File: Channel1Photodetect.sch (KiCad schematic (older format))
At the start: 9 parts, among them U201 MCP6404, U202 LM339

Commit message: revised feedback resistor and updated reference voltage divider
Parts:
- removed R202: 22M, Resistors_SMD:R_0805_HandSoldering, symbol R_Small
- C202: value 2.2p -> 50p; Fieldname (none) -> Value
- R201: value 22M -> 2M; Fieldname (none) -> Value; MPN RMCF0805FT22M0 -> (none)
- renumbered R203 to R202
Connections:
- net at R201.1: now also C202.1, R202.2, U201.1, U202.5 (+)
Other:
- moved on the sheet: R201
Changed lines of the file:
@@
 L R_Small R201
 U 1 1 58228B7C
-P 5040 2480
-F 0 "R201" V 5120 2440 50  0000 L CNN
-F 1 "22M" V 4970 2360 50  0000 L CNN
-F 2 "Resistors_SMD:R_0805_HandSoldering" H 5040 2480 50  0001 C CNN
-F 3 "" H 5040 2480 50  0000 C CNN
-F 4 "RMCF0805FT22M0" H 5040 2480 60  0001 C CNN "MPN"
-	1    5040 2480
+P 5280 2480
+F 0 "R201" V 5360 2440 50  0000 L CNN
+F 1 "2M" V 5210 2360 50  0000 L CNN
+F 2 "Resistors_SMD:R_0805_HandSoldering" H 5280 2480 50  0001 C CNN
+F 3 "" H 5280 2480 50  0000 C CNN
+F 4 "Value" H 5280 2480 60  0001 C CNN "Fieldname"
+	1    5280 2480
 	0    1    1    0
 $EndComp
@@
 P 5270 1990
 F 0 "C202" V 5390 1950 50  0000 L CNN
-F 1 "2.2p" V 5160 1860 50  0000 L CNN
+F 1 "50p" V 5160 1860 50  0000 L CNN
 F 2 "Capacitors_SMD:C_0805_HandSoldering" H 5270 1990 50  0001 C CNN
 F 3 "" H 5270 1990 50  0000 C CNN
+F 4 "Value" H 5270 1990 60  0001 C CNN "Fieldname"
 	1    5270 1990
 	0    1    1    0
@@
 	4860 3140 4860 3440
 $Comp
-L R_Small R203
+L R_Small R202
 U 1 1 58228BA3
 P 5670 3440
-F 0 "R203" V 5750 3400 50  0000 L CNN
+F 0 "R202" V 5750 3400 50  0000 L CNN
 F 1 "10K" V 5600 3320 50  0000 L CNN
 F 2 "Resistors_SMD:R_0805_HandSoldering" H 5670 3440 50  0001 C CNN
@@
 Wire Wire Line
 	6820 3140 7070 3140
-$Comp
-L R_Small R202
-U 1 1 5823C31A
-P 5370 2480
-F 0 "R202" V 5450 2440 50  0000 L CNN
-F 1 "22M" V 5300 2360 50  0000 L CNN
-F 2 "Resistors_SMD:R_0805_HandSoldering" H 5370 2480 50  0001 C CNN
-F 3 "" H 5370 2480 50  0000 C CNN
-F 4 "RMCF0805FT22M0" H 5370 2480 60  0001 C CNN "MPN"
-	1    5370 2480
-	0    1    1    0
-$EndComp
-Wire Wire Line
-	5470 2480 5670 2480
 Connection ~ 5670 2480
 Wire Wire Line
-	5270 2480 5140 2480
-Wire Wire Line
-	4940 2480 4860 2480
+	5670 2480 5380 2480
+Wire Wire Line
+	5180 2480 4860 2480
 Connection ~ 4860 2480
 $EndSCHEMATC

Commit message: added pull-up resistors
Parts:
- added R203: 10K, Resistors_SMD:R_0805_HandSoldering, symbol R_Small
- R201: Fieldname Value -> (none); MPN (none) -> RC0805FR-072ML
- U202: Fieldname (none) -> Value; MPN (none) -> LM339DE4
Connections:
- net +3V: now also R203.2
- net PD1: now also R203.1
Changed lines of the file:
@@
 F 2 "Resistors_SMD:R_0805_HandSoldering" H 5280 2480 50  0001 C CNN
 F 3 "" H 5280 2480 50  0000 C CNN
-F 4 "Value" H 5280 2480 60  0001 C CNN "Fieldname"
+F 4 "RC0805FR-072ML" H 5280 2480 60  0001 C CNN "MPN"
 	1    5280 2480
 	0    1    1    0
@@
 F 1 "LM339" H 6620 2940 50  0000 C CNN
 F 2 "Housings_SOIC:SOIC-14_3.9x8.7mm_Pitch1.27mm" H 6470 3240 50  0001 C CNN
-F 3 "" H 6570 3340 50  0000 C CNN
+F 3 "http://www.ti.com/lit/ds/symlink/lm139a.pdf" H 6570 3340 50  0001 C CNN
+F 4 "Value" H 6520 3140 60  0001 C CNN "Fieldname"
+F 5 "LM339DE4" H 6520 3140 60  0001 C CNN "MPN"
 	1    6520 3140
 	1    0    0    -1
@@
 	5180 2480 4860 2480
 Connection ~ 4860 2480
+$Comp
+L R_Small R203
+U 1 1 5824D012
+P 6990 2890
+F 0 "R203" V 7070 2850 50  0000 L CNN
+F 1 "10K" V 6920 2770 50  0000 L CNN
+F 2 "Resistors_SMD:R_0805_HandSoldering" H 6990 2890 50  0001 C CNN
+F 3 "" H 6990 2890 50  0000 C CNN
+F 4 "RC0805FR-072ML" H 6990 2890 60  0001 C CNN "MPN"
+	1    6990 2890
+	-1   0    0    1
+$EndComp
+Text GLabel 6990 2640 1    60   Input ~ 0
++3V
+Wire Wire Line
+	6990 2640 6990 2790
+Wire Wire Line
+	6990 2990 6990 3140
+Connection ~ 6990 3140
 $EndSCHEMATC

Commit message: removed 10K resistors used as load for op amps
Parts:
- removed R202: 10K, Resistors_SMD:R_0805_HandSoldering, symbol R_Small
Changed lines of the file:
@@
 	5170 1990 4860 1990
-Wire Wire Line
-	5670 1990 5670 3340
 Wire Wire Line
 	5460 3040 6220 3040
@@
 	4860 3140 4860 3440
 $Comp
-L R_Small R202
-U 1 1 58228BA3
-P 5670 3440
-F 0 "R202" V 5750 3400 50  0000 L CNN
-F 1 "10K" V 5600 3320 50  0000 L CNN
-F 2 "Resistors_SMD:R_0805_HandSoldering" H 5670 3440 50  0001 C CNN
-F 3 "" H 5670 3440 50  0000 C CNN
-F 4 "Value" H 5670 3440 60  0001 C CNN "Fieldname"
-	1    5670 3440
-	-1   0    0    1
-$EndComp
-Connection ~ 5670 3040
-$Comp
-L GND #PWR06
-U 1 1 58228BAB
-P 5670 3640
-F 0 "#PWR06" H 5670 3390 50  0001 C CNN
-F 1 "GND" H 5670 3490 50  0000 C CNN
-F 2 "" H 5670 3640 50  0000 C CNN
-F 3 "" H 5670 3640 50  0000 C CNN
-	1    5670 3640
-	1    0    0    -1
-$EndComp
-Wire Wire Line
-	5670 3540 5670 3640
-$Comp
 L LM339 U202
 U 1 1 58228BB2
@@
 $EndComp
 $Comp
-L GND #PWR07
+L GND #PWR06
 U 1 1 58228BCA
 P 5060 3450
-F 0 "#PWR07" H 5060 3200 50  0001 C CNN
+F 0 "#PWR06" H 5060 3200 50  0001 C CNN
 F 1 "GND" H 5060 3300 50  0000 C CNN
 F 2 "" H 5060 3450 50  0000 C CNN
@@
 $EndComp
 $Comp
-L GND #PWR08
+L GND #PWR07
 U 1 1 58228BD8
 P 4170 2540
-F 0 "#PWR08" H 4170 2290 50  0001 C CNN
+F 0 "#PWR07" H 4170 2290 50  0001 C CNN
 F 1 "GND" H 4170 2390 50  0000 C CNN
 F 2 "" H 4170 2540 50  0000 C CNN
@@
 	4250 2940 4860 2940
 $Comp
-L GND #PWR09
+L GND #PWR08
 U 1 1 58228BED
 P 4300 3400
-F 0 "#PWR09" H 4300 3150 50  0001 C CNN
+F 0 "#PWR08" H 4300 3150 50  0001 C CNN
 F 1 "GND" H 4300 3250 50  0000 C CNN
 F 2 "" H 4300 3400 50  0000 C CNN
@@
 +3V
 $Comp
-L GND #PWR010
+L GND #PWR09
 U 1 1 58228BF6
 P 6420 3440
-F 0 "#PWR010" H 6420 3190 50  0001 C CNN
+F 0 "#PWR09" H 6420 3190 50  0001 C CNN
 F 1 "GND" H 6420 3290 50  0000 C CNN
 F 2 "" H 6420 3440 50  0000 C CNN
@@
 $EndComp
 $Comp
-L GND #PWR011
+L GND #PWR010
 U 1 1 58228C05
 P 5980 2550
-F 0 "#PWR011" H 5980 2300 50  0001 C CNN
+F 0 "#PWR010" H 5980 2300 50  0001 C CNN
 F 1 "GND" H 5980 2400 50  0000 C CNN
 F 2 "" H 5980 2550 50  0000 C CNN
@@
 Wire Wire Line
 	6820 3140 7070 3140
-Connection ~ 5670 2480
-Wire Wire Line
-	5670 2480 5380 2480
 Wire Wire Line
 	5180 2480 4860 2480
@@
 	6990 2990 6990 3140
 Connection ~ 6990 3140
+Wire Wire Line
+	5380 2480 5680 2480
+Wire Wire Line
+	5680 2480 5680 3040
+Connection ~ 5680 3040
+Wire Wire Line
+	5670 1990 5670 2480
+Connection ~ 5670 2480
 $EndSCHEMATC

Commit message: replaced potentiometer with trimpot
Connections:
- net GND: now also U201.13 (-); no longer U201.2 (-)
- net at C202.1, R201.1, U202.5 (+): now also U201.14; no longer U201.1
- net at C202.2, PD201.1 (K), R201.2: now also U201.12 (+); no longer U201.3 (+)
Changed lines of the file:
@@
 $Comp
 L MCP6404 U201
-U 1 1 58228B8A
+U 4 1 58228B8A
 P 5160 3040
 F 0 "U201" H 5210 3240 50  0000 C CNN
@@
 F 4 "MCP6404-E/SL" H 5160 3040 60  0001 C CNN "MPN"
 F 5 "Value" H 5160 3040 60  0001 C CNN "Fieldname"
-	1    5160 3040
+	4    5160 3040
 	1    0    0    -1
 $EndComp

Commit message: completed pcb basic layout
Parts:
- renumbered R203 to R202
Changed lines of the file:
@@
 	5370 1990 5670 1990
 $Comp
-L GND #PWR05
+L GND #PWR203
 U 1 1 58228B9B
 P 4860 3440
-F 0 "#PWR05" H 4860 3190 50  0001 C CNN
+F 0 "#PWR203" H 4860 3190 50  0001 C CNN
 F 1 "GND" H 4860 3290 50  0000 C CNN
 F 2 "" H 4860 3440 50  0000 C CNN
@@
 $EndComp
 $Comp
-L GND #PWR06
+L GND #PWR204
 U 1 1 58228BCA
 P 5060 3450
-F 0 "#PWR06" H 5060 3200 50  0001 C CNN
+F 0 "#PWR204" H 5060 3200 50  0001 C CNN
 F 1 "GND" H 5060 3300 50  0000 C CNN
 F 2 "" H 5060 3450 50  0000 C CNN
@@
 $EndComp
 $Comp
-L GND #PWR07
+L GND #PWR201
 U 1 1 58228BD8
 P 4170 2540
-F 0 "#PWR07" H 4170 2290 50  0001 C CNN
+F 0 "#PWR201" H 4170 2290 50  0001 C CNN
 F 1 "GND" H 4170 2390 50  0000 C CNN
 F 2 "" H 4170 2540 50  0000 C CNN
@@
 	4250 2940 4860 2940
 $Comp
-L GND #PWR08
+L GND #PWR202
 U 1 1 58228BED
 P 4300 3400
-F 0 "#PWR08" H 4300 3150 50  0001 C CNN
+F 0 "#PWR202" H 4300 3150 50  0001 C CNN
 F 1 "GND" H 4300 3250 50  0000 C CNN
 F 2 "" H 4300 3400 50  0000 C CNN
@@
 +3V
 $Comp
-L GND #PWR09
+L GND #PWR206
 U 1 1 58228BF6
 P 6420 3440
-F 0 "#PWR09" H 6420 3190 50  0001 C CNN
+F 0 "#PWR206" H 6420 3190 50  0001 C CNN
 F 1 "GND" H 6420 3290 50  0000 C CNN
 F 2 "" H 6420 3440 50  0000 C CNN
@@
 $EndComp
 $Comp
-L GND #PWR010
+L GND #PWR205
 U 1 1 58228C05
 P 5980 2550
-F 0 "#PWR010" H 5980 2300 50  0001 C CNN
+F 0 "#PWR205" H 5980 2300 50  0001 C CNN
 F 1 "GND" H 5980 2400 50  0000 C CNN
 F 2 "" H 5980 2550 50  0000 C CNN
@@
 Connection ~ 4860 2480
 $Comp
-L R_Small R203
+L R_Small R202
 U 1 1 5824D012
 P 6990 2890
-F 0 "R203" V 7070 2850 50  0000 L CNN
+F 0 "R202" V 7070 2850 50  0000 L CNN
 F 1 "10K" V 6920 2770 50  0000 L CNN
 F 2 "Resistors_SMD:R_0805_HandSoldering" H 6990 2890 50  0001 C CNN

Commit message: changed photodiodes to BPW 34 S due to availability. Changed feedbak resistor and cap due to increased current output of diode.
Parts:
- C202: value 50p -> 100p
- PD201: value VBPW34S -> BPW 34 S-Z; AltPart (none) -> VBPW34S
- R201: value 2M -> 1M; Fieldname (none) -> Value; MPN RC0805FR-072ML -> (none)
- R202: Fieldname (none) -> Value; MPN RC0805FR-072ML -> (none)
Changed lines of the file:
@@
 P 5280 2480
 F 0 "R201" V 5360 2440 50  0000 L CNN
-F 1 "2M" V 5210 2360 50  0000 L CNN
+F 1 "1M" V 5210 2360 50  0000 L CNN
 F 2 "Resistors_SMD:R_0805_HandSoldering" H 5280 2480 50  0001 C CNN
 F 3 "" H 5280 2480 50  0000 C CNN
-F 4 "RC0805FR-072ML" H 5280 2480 60  0001 C CNN "MPN"
+F 4 "Value" H 5280 2480 60  0001 C CNN "Fieldname"
+F 5 "  " H 5280 2480 60  0001 C CNN "MPN"
 	1    5280 2480
 	0    1    1    0
@@
 P 5270 1990
 F 0 "C202" V 5390 1950 50  0000 L CNN
-F 1 "50p" V 5160 1860 50  0000 L CNN
+F 1 "100p" V 5160 1860 50  0000 L CNN
 F 2 "Capacitors_SMD:C_0805_HandSoldering" H 5270 1990 50  0001 C CNN
 F 3 "" H 5270 1990 50  0000 C CNN
@@
 	5370 1990 5670 1990
 $Comp
-L GND #PWR203
+L GND #PWR05
 U 1 1 58228B9B
 P 4860 3440
-F 0 "#PWR203" H 4860 3190 50  0001 C CNN
+F 0 "#PWR05" H 4860 3190 50  0001 C CNN
 F 1 "GND" H 4860 3290 50  0000 C CNN
 F 2 "" H 4860 3440 50  0000 C CNN
@@
 $EndComp
 $Comp
-L GND #PWR204
+L GND #PWR06
 U 1 1 58228BCA
 P 5060 3450
-F 0 "#PWR204" H 5060 3200 50  0001 C CNN
+F 0 "#PWR06" H 5060 3200 50  0001 C CNN
 F 1 "GND" H 5060 3300 50  0000 C CNN
 F 2 "" H 5060 3450 50  0000 C CNN
@@
 $EndComp
 $Comp
-L GND #PWR201
+L GND #PWR07
 U 1 1 58228BD8
 P 4170 2540
-F 0 "#PWR201" H 4170 2290 50  0001 C CNN
+F 0 "#PWR07" H 4170 2290 50  0001 C CNN
 F 1 "GND" H 4170 2390 50  0000 C CNN
 F 2 "" H 4170 2540 50  0000 C CNN
@@
 P 4250 3150
 F 0 "PD201" H 4170 3230 50  0000 L CNN
-F 1 "VBPW34S" H 4100 3070 50  0000 L CNN
+F 1 "BPW 34 S-Z" H 4100 3070 50  0000 L CNN
 F 2 "DasBlinkinput:VBPW34S" V 4250 3150 50  0001 C CNN
-F 3 "http://www.vishay.com/docs/81128/vbpw34s.pdf" V 4250 3150 50  0001 C CNN
+F 3 "http://media.digikey.com/pdf/Data%20Sheets/Osram%20PDFs/bpw34_spdf.pdf" V 4250 3150 50  0001 C CNN
 F 4 "Value" H 4250 3150 60  0001 C CNN "Fieldname"
+F 5 "VBPW34S" H 4250 3150 60  0001 C CNN "AltPart"
 	1    4250 3150
 	0    1    1    0
@@
 	4250 2940 4860 2940
 $Comp
-L GND #PWR202
+L GND #PWR08
 U 1 1 58228BED
 P 4300 3400
-F 0 "#PWR202" H 4300 3150 50  0001 C CNN
+F 0 "#PWR08" H 4300 3150 50  0001 C CNN
 F 1 "GND" H 4300 3250 50  0000 C CNN
 F 2 "" H 4300 3400 50  0000 C CNN
@@
 +3V
 $Comp
-L GND #PWR206
+L GND #PWR09
 U 1 1 58228BF6
 P 6420 3440
-F 0 "#PWR206" H 6420 3190 50  0001 C CNN
+F 0 "#PWR09" H 6420 3190 50  0001 C CNN
 F 1 "GND" H 6420 3290 50  0000 C CNN
 F 2 "" H 6420 3440 50  0000 C CNN
@@
 $EndComp
 $Comp
-L GND #PWR205
+L GND #PWR010
 U 1 1 58228C05
 P 5980 2550
-F 0 "#PWR205" H 5980 2300 50  0001 C CNN
+F 0 "#PWR010" H 5980 2300 50  0001 C CNN
 F 1 "GND" H 5980 2400 50  0000 C CNN
 F 2 "" H 5980 2550 50  0000 C CNN
@@
 F 2 "Resistors_SMD:R_0805_HandSoldering" H 6990 2890 50  0001 C CNN
 F 3 "" H 6990 2890 50  0000 C CNN
-F 4 "RC0805FR-072ML" H 6990 2890 60  0001 C CNN "MPN"
+F 4 "Value" H 6990 2890 60  0001 C CNN "Fieldname"
 	1    6990 2890
 	-1   0    0    1

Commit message: added test points at outputs of op-amps
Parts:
- added P201: CONN_01X01, Pin_Headers:Pin_Header_Straight_1x01, symbol CONN_01X01
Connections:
- net at C202.1, R201.1, U201.14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: now also P201.1 (P1)
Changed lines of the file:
@@
 	5670 1990 5670 2480
 Connection ~ 5670 2480
+$Comp
+L CONN_01X01 P201
+U 1 1 585443E6
+P 5870 3330
+F 0 "P201" H 5820 3430 50  0000 C CNN
+F 1 "CONN_01X01" V 5970 3330 50  0000 C CNN
+F 2 "Pin_Headers:Pin_Header_Straight_1x01" H 5870 3330 50  0001 C CNN
+F 3 "" H 5870 3330 50  0000 C CNN
+	1    5870 3330
+	0    1    1    0
+$EndComp
+Wire Wire Line
+	5870 3130 5870 3040
+Connection ~ 5870 3040
 $EndSCHEMATC

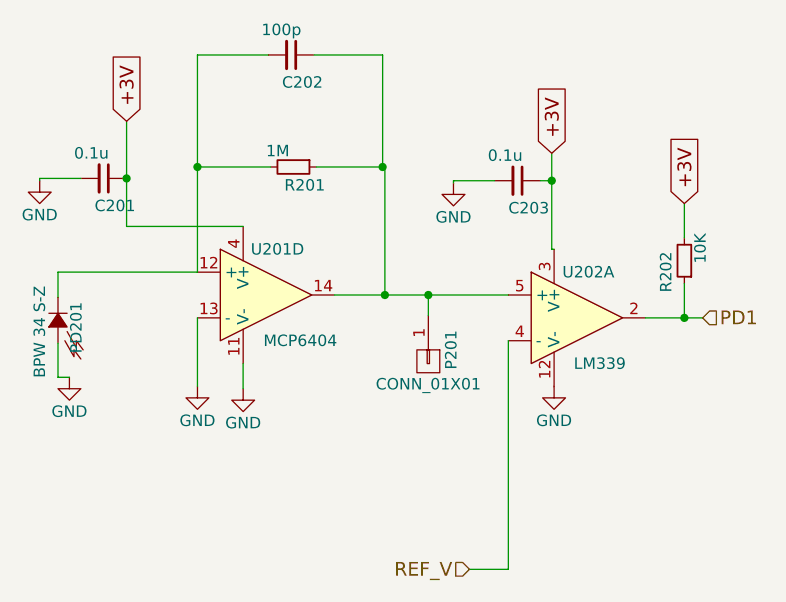
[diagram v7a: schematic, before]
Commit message: corrected inputs on opamp and rerouted traces
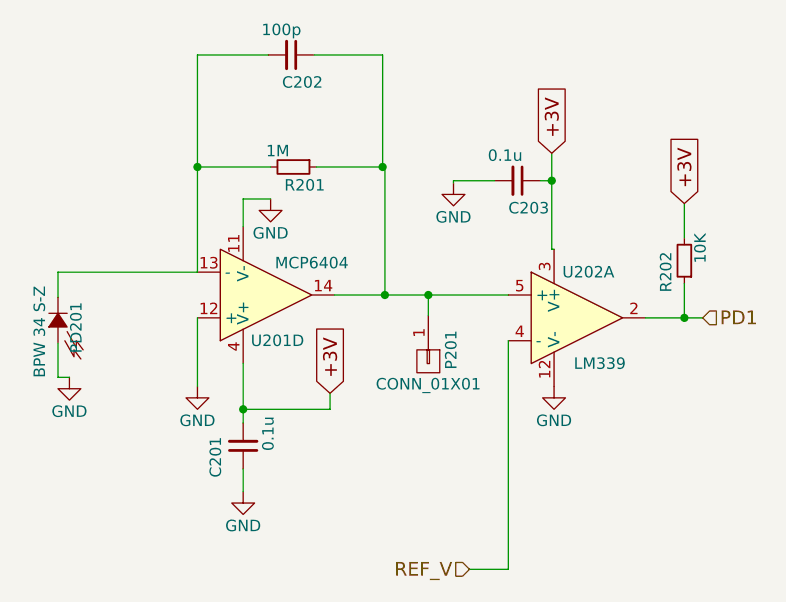
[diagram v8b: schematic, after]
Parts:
- U201, U202: footprint Housings_SOIC:SOIC-14_3.9x8.7mm_Pitch1.27mm -> DasBlinkinput:SOIC-14_3.9x8.7mm_Pitch1.27mm
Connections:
- net +3V: now also C201.2; no longer C201.1
- net GND: now also C201.1, U201.12 (+); no longer C201.2, U201.13 (-)
- net at C202.2, PD201.1 (K), R201.2: now also U201.13 (-); no longer U201.12 (+)
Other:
- moved on the sheet: C201
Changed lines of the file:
@@
 P 5160 3040
 F 0 "U201" H 5210 3240 50  0000 C CNN
-F 1 "MCP6404" H 5310 2840 50  0000 C CNN
-F 2 "Housings_SOIC:SOIC-14_3.9x8.7mm_Pitch1.27mm" H 5110 3140 50  0001 C CNN
+F 1 "MCP6404" H 5360 2900 50  0000 C CNN
+F 2 "DasBlinkinput:SOIC-14_3.9x8.7mm_Pitch1.27mm" H 5110 3140 50  0001 C CNN
 F 3 "http://ww1.microchip.com/downloads/en/DeviceDoc/22229D.pdf" H 5210 3240 50  0001 C CNN
 F 4 "MCP6404-E/SL" H 5160 3040 60  0001 C CNN "MPN"
 F 5 "Value" H 5160 3040 60  0001 C CNN "Fieldname"
 	4    5160 3040
-	1    0    0    -1
+	1    0    0    1
 $EndComp
 Wire Wire Line
@@
 F 0 "U202" H 6570 3340 50  0000 C CNN
 F 1 "LM339" H 6620 2940 50  0000 C CNN
-F 2 "Housings_SOIC:SOIC-14_3.9x8.7mm_Pitch1.27mm" H 6470 3240 50  0001 C CNN
+F 2 "DasBlinkinput:SOIC-14_3.9x8.7mm_Pitch1.27mm" H 6470 3240 50  0001 C CNN
 F 3 "http://www.ti.com/lit/ds/symlink/lm139a.pdf" H 6570 3340 50  0001 C CNN
 F 4 "Value" H 6520 3140 60  0001 C CNN "Fieldname"
@@
 L GND #PWR06
 U 1 1 58228BCA
-P 5060 3450
-F 0 "#PWR06" H 5060 3200 50  0001 C CNN
-F 1 "GND" H 5060 3300 50  0000 C CNN
-F 2 "" H 5060 3450 50  0000 C CNN
-F 3 "" H 5060 3450 50  0000 C CNN
-	1    5060 3450
-	1    0    0    -1
-$EndComp
-Wire Wire Line
-	5060 3340 5060 3450
+P 5180 2620
+F 0 "#PWR06" H 5180 2370 50  0001 C CNN
+F 1 "GND" H 5180 2470 50  0000 C CNN
+F 2 "" H 5180 2620 50  0000 C CNN
+F 3 "" H 5180 2620 50  0000 C CNN
+	1    5180 2620
+	1    0    0    -1
+$EndComp
 $Comp
 L C_Small C201
 U 1 1 58228BD1
-P 4450 2530
-F 0 "C201" V 4570 2490 50  0000 L CNN
-F 1 "0.1u" V 4340 2400 50  0000 L CNN
-F 2 "Capacitors_SMD:C_0805_HandSoldering" H 4450 2530 50  0001 C CNN
-F 3 "" H 4450 2530 50  0000 C CNN
-	1    4450 2530
-	0    1    1    0
+P 5060 3700
+F 0 "C201" V 5180 3660 50  0000 L CNN
+F 1 "0.1u" V 4950 3570 50  0000 L CNN
+F 2 "Capacitors_SMD:C_0805_HandSoldering" H 5060 3700 50  0001 C CNN
+F 3 "" H 5060 3700 50  0000 C CNN
+	1    5060 3700
+	-1   0    0    1
 $EndComp
 $Comp
 L GND #PWR07
 U 1 1 58228BD8
-P 4170 2540
-F 0 "#PWR07" H 4170 2290 50  0001 C CNN
-F 1 "GND" H 4170 2390 50  0000 C CNN
-F 2 "" H 4170 2540 50  0000 C CNN
-F 3 "" H 4170 2540 50  0000 C CNN
-	1    4170 2540
-	1    0    0    -1
-$EndComp
-Wire Wire Line
-	4350 2530 4170 2530
-Wire Wire Line
-	4170 2530 4170 2540
-Wire Wire Line
-	4550 2280 4550 2740
-Wire Wire Line
-	4550 2740 5060 2740
-Connection ~ 4550 2530
-Text GLabel 4550 2280 1    60   Input ~ 0
+P 5060 3900
+F 0 "#PWR07" H 5060 3650 50  0001 C CNN
+F 1 "GND" H 5060 3750 50  0000 C CNN
+F 2 "" H 5060 3900 50  0000 C CNN
+F 3 "" H 5060 3900 50  0000 C CNN
+	1    5060 3900
+	1    0    0    -1
+$EndComp
+Text GLabel 5440 3470 1    60   Input ~ 0
 +3V
 $Comp
@@
 	5870 3130 5870 3040
 Connection ~ 5870 3040
+Wire Wire Line
+	5180 2620 5060 2620
+Wire Wire Line
+	5060 2620 5060 2740
+Wire Wire Line
+	5060 3340 5060 3600
+Wire Wire Line
+	5440 3470 5440 3540
+Wire Wire Line
+	5440 3540 5060 3540
+Connection ~ 5060 3540
+Wire Wire Line
+	5060 3800 5060 3900
 $EndSCHEMATC
